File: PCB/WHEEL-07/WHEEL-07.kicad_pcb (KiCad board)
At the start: 4 copper layers, 52.5 x 34.7 mm, 94 parts, among them IC2 LDO40LPU50RY, IC3 MP2332HGTL-P, IC4 NL27WZ14DTT1G, J1 Conn_01x06_Male, J10 BUTTON, J11 DBG, J12 Conn_01x10, J14 BUTTON, J15 BUTTON, J16 POWER, J17 TIM, J2 Conn_01x06_Male, J5 Conn_01x04_Male, J7 BUTTON, J8 BUTTON, J9 BUTTON, Q1 AO3401A, U1 STM32F405RGTx, U2 MCP2561-E-SN, U3 MCP2561-E-SN, Y1 16Mhz, Y2 32KHz

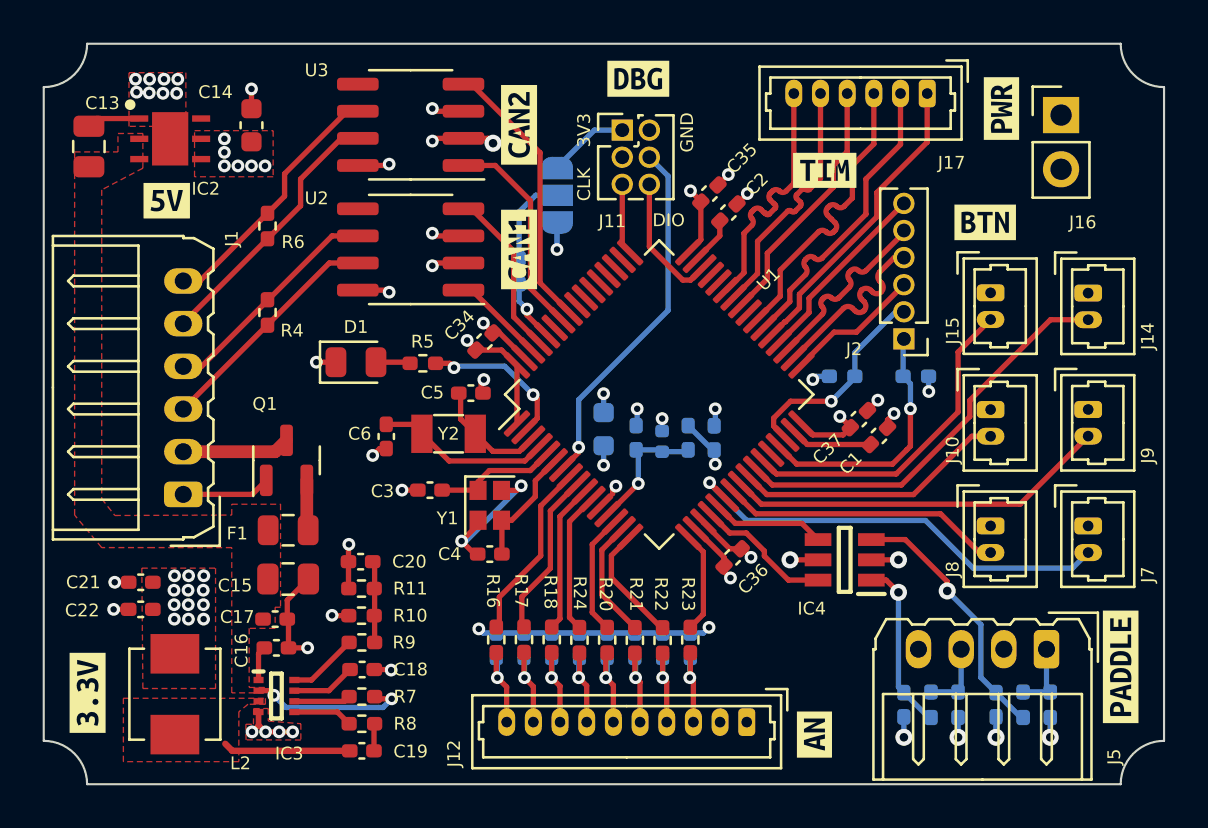
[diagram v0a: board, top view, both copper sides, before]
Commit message: Changed power supply section for 2 x LDO40
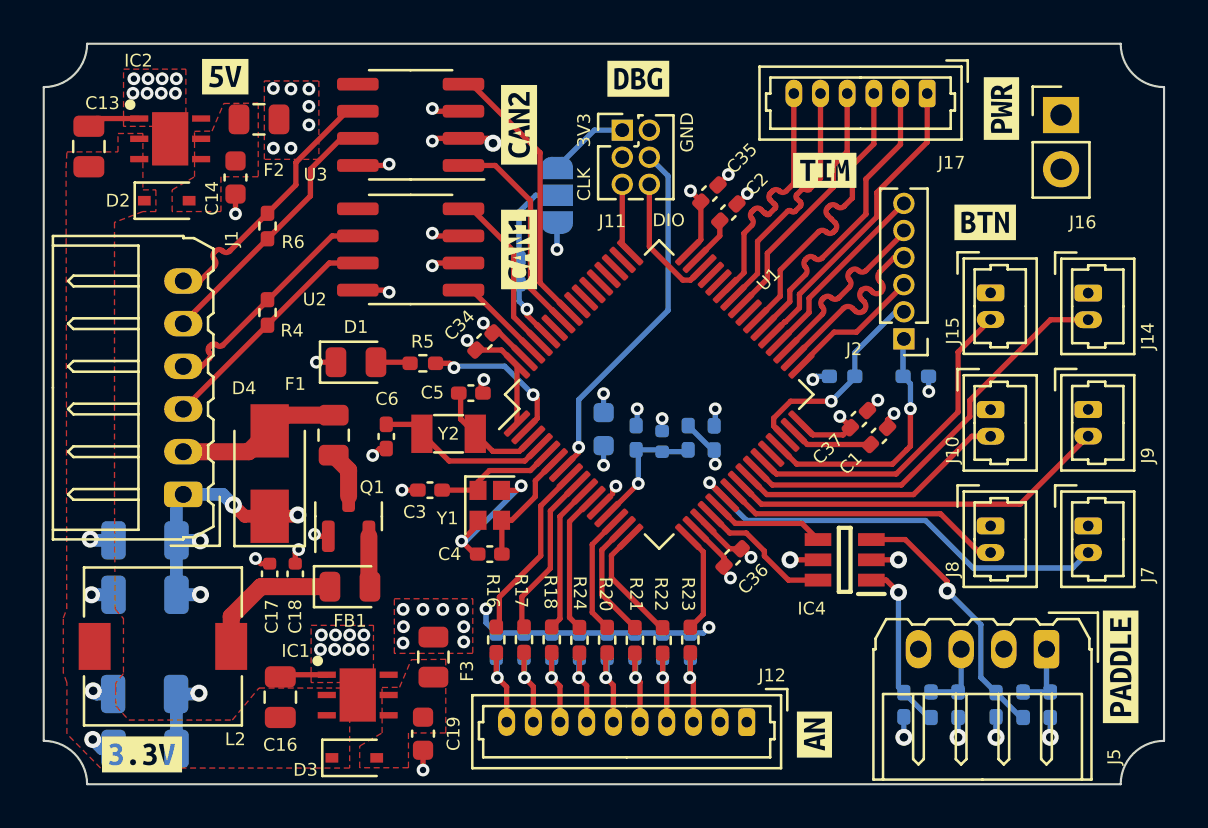
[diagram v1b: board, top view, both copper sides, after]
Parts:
- removed C20: 10pF, Capacitor_SMD:C_0402_1005Metric_Pad0.74x0.62mm_HandSolder
- removed C21, C22: 22uF, Capacitor_SMD:C_0402_1005Metric_Pad0.74x0.62mm_HandSolder
- removed IC3: MP2332HGTL-P, WHEEL_07_LIBRARY_LOADER:SOTFL50P160X60-8N
- removed R10: 13k, Resistor_SMD:R_0402_1005Metric_Pad0.72x0.64mm_HandSolder
- removed R11: 40.2k, Resistor_SMD:R_0402_1005Metric_Pad0.72x0.64mm_HandSolder
- removed R7: 200k, Resistor_SMD:R_0402_1005Metric_Pad0.72x0.64mm_HandSolder
- removed R8: 20, Resistor_SMD:R_0402_1005Metric_Pad0.72x0.64mm_HandSolder
- removed R9: 20k, Resistor_SMD:R_0402_1005Metric_Pad0.72x0.64mm_HandSolder
- added C10: 10uF, Capacitor_SMD:C_1206_3216Metric, B.Cu at (153.2, 83.6)
- added C11: 10uF, Capacitor_SMD:C_1206_3216Metric, B.Cu at (153.2, 76.4)
- added C12: 10uF, Capacitor_SMD:C_1206_3216Metric, B.Cu at (153.2, 73.8)
- added D2: 1N4448WS, Diode_SMD:D_SOD-323, F.Cu at (154.2, 57.9)
- added D3: 1N4448WS, Diode_SMD:D_SOD-323, F.Cu at (163.0, 84.0)
- added D4: D_TVS, Diode_SMD:D_SMA, F.Cu at (159.0, 70.7)
- added F2: 100mA, Fuse:Fuse_0805_2012Metric, F.Cu at (158.5, 54.1)
- added F3: 100mA, Fuse:Fuse_0805_2012Metric, F.Cu at (166.7, 79.3)
- added FB1: 110E, LED_SMD:LED_0805_2012Metric, F.Cu at (162.8, 76.0)
- added IC1: LDO40LPU33RY, PDMS_Additional:SON95P300X300X90-7N-D, F.Cu at (163.1, 81.1)
- C15: value 22uF -> 10uF; footprint Capacitor_SMD:C_0805_2012Metric -> Capacitor_SMD:C_1206_3216Metric; moved to B.Cu
- C16: value 1nF -> 1uF; footprint Capacitor_SMD:C_0402_1005Metric_Pad0.74x0.62mm_HandSolder -> Capacitor_SMD:C_0805_2012Metric
- C17: value 0.1uF -> 100pF / 50V; footprint Capacitor_SMD:C_0402_1005Metric_Pad0.74x0.62mm_HandSolder -> Capacitor_SMD:C_0402_1005Metric
- C18: value 6.8nF -> 100nF/50V; footprint Capacitor_SMD:C_0402_1005Metric_Pad0.74x0.62mm_HandSolder -> Capacitor_SMD:C_0402_1005Metric
- C19: value 1uF -> 4.7uF; footprint Capacitor_SMD:C_0402_1005Metric_Pad0.74x0.62mm_HandSolder -> Capacitor_SMD:C_0603_1608Metric
- F1: value Fuse -> 500mA
- L2: value 2.2uH -> 120uH / 0.5A; footprint Inductor_SMD:L_Vishay_IHLP-1616 -> Inductor_SMD:L_7.3x7.3_H4.5
- moved C15 8.62 mm to (153.1, 81.0)
- moved kibuzzard-64076DFA 6.43 mm to (156.9, 52.1)
- moved C18 5.47 mm to (160.2, 75.4), turned to 90 degrees
- moved F1 4.94 mm to (162.0, 68.9), turned to -90 degrees
- moved Q1 3.92 mm to (162.7, 72.7)
- moved kibuzzard-64076DF0 3.85 mm to (153.0, 83.9), turned to 0 degrees
- moved C19 2.98 mm to (166.2, 82.9), turned to -90 degrees
- moved C14 2.56 mm to (157.4, 56.8), turned to -90 degrees
- moved C16 2.32 mm to (159.5, 81.2), turned to 90 degrees
- moved L2 2.31 mm to (154.0, 78.8), turned to 0 degrees
- moved C17 2.14 mm to (159.0, 75.4), turned to 90 degrees
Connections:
- C14 pad 1: +5V -> /POWER/5VPREFUSE
- C16 pad 1: GND -> +12V
- C16 pad 2: /POWER/PG3V3 -> GND
- C17 pad 1: GND -> Net-(C17-Pad1)
- C17 pad 2: +12V -> GND
- C18 pad 1: GND -> Net-(C17-Pad1)
- C18 pad 2: Net-(C18-Pad2) -> GND
- C19 pad 1: Net-(C19-Pad1) -> /POWER/3V3PREFUSE
- C19 pad 2: Net-(C19-Pad2) -> GND
- F1 pad 1: +12V -> 12V_CONN
- F1 pad 2: Net-(F1-Pad2) -> Net-(Q1-Pad3)
- IC2 pad 4: +5V -> /POWER/5VPREFUSE
- IC2 pad 5: +5V -> /POWER/5VPREFUSE
- L2 pad 1: Net-(C19-Pad2) -> +12V
- L2 pad 2: +3.3V -> Net-(C17-Pad1)
- Q1 pad 2: Net-(F1-Pad2) -> Net-(Q1-Pad2)
- Q1 pad 3: 12V_CONN -> Net-(Q1-Pad3)
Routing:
- net GND: track 64.6 -> 71.7 mm, vias 45 -> 53
- net Net-(C17-Pad1): track 0.00 -> 6.61 mm
- net Net-(C19-Pad2): track 5.97 -> 0.00 mm
- net Net-(C20-Pad1): track 3.82 -> 0.00 mm
- net Net-(IC3-Pad8): track 3.30 -> 0.00 mm
- net +12V: track 7.58 -> 4.31 mm, vias 2 -> 4
- net Net-(C18-Pad2): track 3.02 -> 0.00 mm
- net Net-(IC3-Pad5): track 2.80 -> 0.00 mm
- net 12V_CONN: track 5.06 -> 7.76 mm
- net Net-(IC3-Pad6): track 2.66 -> 0.00 mm
- net Net-(Q1-Pad2): track 0.00 -> 2.38 mm
- net Net-(F1-Pad2): track 2.37 -> 0.00 mm
- net Net-(Q1-Pad3): track 0.00 -> 2.21 mm
- net +3.3V: track 28.1 -> 26.0 mm, vias 25 -> 20
- net /POWER/PG3V3: track 1.62 -> 0.00 mm
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- added copper zone on F.Cu, net /POWER/3V3PREFUSE
- added copper zone on F.Cu, net /POWER/5VPREFUSE
- removed copper zone on F.Cu, net Net-(C19-Pad2)

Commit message: Revised board with 2 x LDO40 and cleaned-up schematics
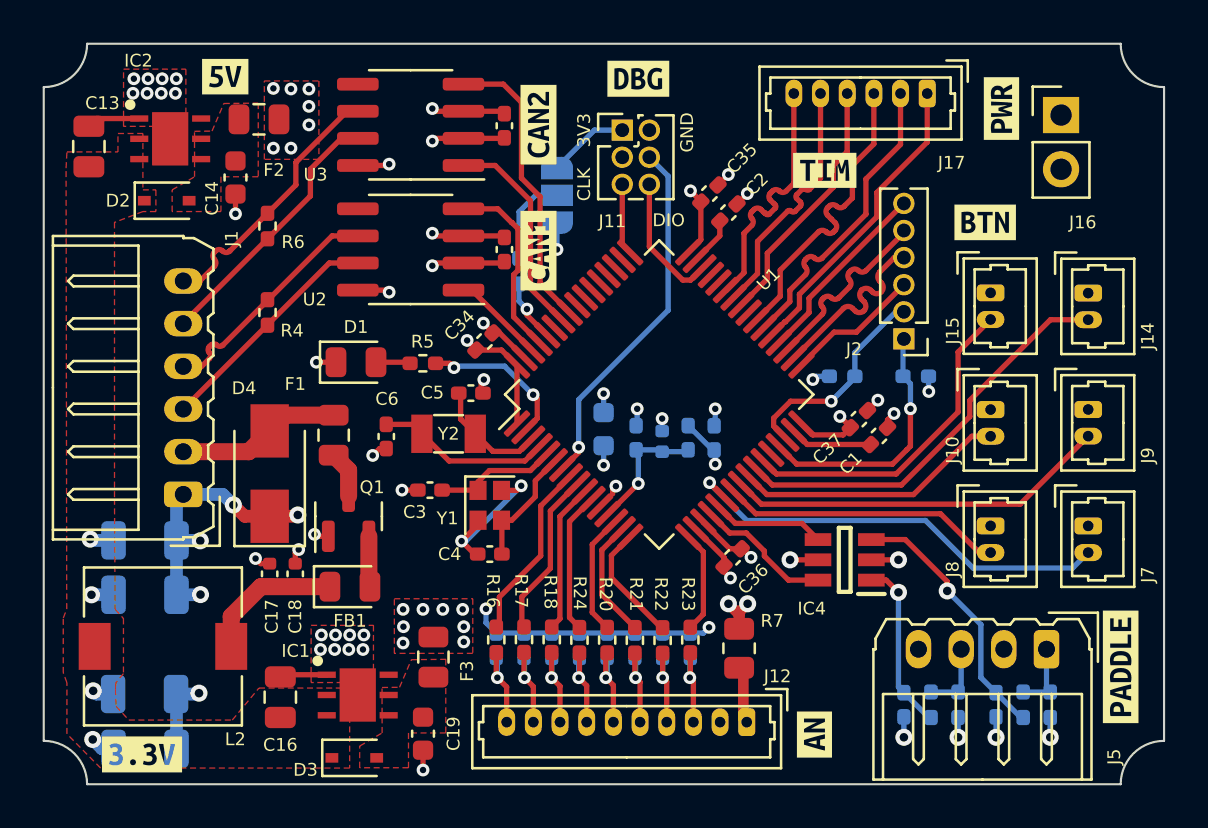
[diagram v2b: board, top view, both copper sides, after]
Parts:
- added C20: 100nF, Capacitor_SMD:C_0402_1005Metric_Pad0.74x0.62mm_HandSolder, F.Cu at (170.0, 54.4)
- added C21: 100nF, Capacitor_SMD:C_0402_1005Metric_Pad0.74x0.62mm_HandSolder, F.Cu at (170.0, 60.2)
- added R7: 10, Resistor_SMD:R_0805_2012Metric, F.Cu at (181.0, 78.9)
- moved kibuzzard-64135F75 0.91 mm to (171.6, 60.2)
- moved kibuzzard-64135F81 0.91 mm to (171.6, 54.4)
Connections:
- J12 pad 1: +3.3V -> Net-(J12-Pad1)
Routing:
- net +5V: track 3.02 -> 6.93 mm
- net +3.3V: track 26.0 -> 28.7 mm, vias 20 -> 22
- net Net-(J12-Pad1): track 0.00 -> 2.69 mm
- net GND: track 71.7 -> 74.1 mm, vias 53 -> 52
- net CAN1_RX: track 7.98 -> 8.88 mm
- net CAN2_RX: track 13.0 -> 13.9 mm
